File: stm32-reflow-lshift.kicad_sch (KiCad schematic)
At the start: 17 parts, among them J6 Conn_02x08_Odd_Even, Q1 2N7002, Q10 2N7002, Q11 2N7002, Q2 2N7002, Q3 2N7002, Q4 2N7002, Q5 2N7002, Q6 2N7002, Q7 2N7002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

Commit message: initial routing, added power supply source
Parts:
- J6: footprint Connector_PinSocket_2.54mm:PinSocket_2x08_P2.54mm_Vertical_SMD -> Connector_IDC:IDC-Header_2x08_P2.54mm_Vertical
- RV1: footprint Potentiometer_SMD:Potentiometer_ACP_CA6-VSMD_Vertical -> Potentiometer_SMD:Potentiometer_Bourns_3314G_Vertical
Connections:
- net DB0: now also RN2.2 (R1); no longer RN2.5 (R4)
- net DB1: now also RN2.3 (R2); no longer RN2.6 (R5)
- net DB2: now also RN2.4 (R3); no longer RN2.7 (R6)
- net DB3: now also RN2.5 (R4); no longer RN2.8 (R7)
- net DB4: now also RN2.6 (R5); no longer RN2.9 (R8)
- net DB5: now also RN2.7 (R6); no longer RN2.10 (R9)
- net DB6: now also RN2.8 (R7); no longer RN2.11 (R10)
- net DB7: now also RN2.9 (R8); no longer RN2.12 (R11)
- net E: now also RN2.12 (R11); no longer RN2.2 (R1)
- net RS: now also RN2.10 (R9); no longer RN2.4 (R3)
- net R/~{W}: now also RN2.11 (R10); no longer RN2.3 (R2)
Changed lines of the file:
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@@
     (effects (font (size 1.27 1.27)) (justify right bottom))
   )
-  (label "E" (at 38.1 110.49 270)
+  (label "DB0" (at 38.1 110.49 270)
     (effects (font (size 1.27 1.27)) (justify right bottom))
   )
@@
     (effects (font (size 1.27 1.27)) (justify left bottom))
   )
-  (label "R{slash}~{W}" (at 40.64 110.49 270)
-    (effects (font (size 1.27 1.27)) (justify right bottom))
-  )
-  (label "RS" (at 43.18 110.49 270)
-    (effects (font (size 1.27 1.27)) (justify right bottom))
-  )
-  (label "DB0" (at 45.72 110.49 270)
-    (effects (font (size 1.27 1.27)) (justify right bottom))
-  )
-  (label "DB1" (at 48.26 110.49 270)
-    (effects (font (size 1.27 1.27)) (justify right bottom))
-  )
-  (label "DB2" (at 50.8 110.49 270)
-    (effects (font (size 1.27 1.27)) (justify right bottom))
-  )
-  (label "DB3" (at 53.34 110.49 270)
-    (effects (font (size 1.27 1.27)) (justify right bottom))
-  )
-  (label "DB4" (at 55.88 110.49 270)
-    (effects (font (size 1.27 1.27)) (justify right bottom))
-  )
-  (label "DB5" (at 58.42 110.49 270)
-    (effects (font (size 1.27 1.27)) (justify right bottom))
-  )
-  (label "DB6" (at 60.96 110.49 270)
-    (effects (font (size 1.27 1.27)) (justify right bottom))
-  )
-  (label "DB7" (at 63.5 110.49 270)
+  (label "DB1" (at 40.64 110.49 270)
+    (effects (font (size 1.27 1.27)) (justify right bottom))
+  )
+  (label "DB2" (at 43.18 110.49 270)
+    (effects (font (size 1.27 1.27)) (justify right bottom))
+  )
+  (label "DB3" (at 45.72 110.49 270)
+    (effects (font (size 1.27 1.27)) (justify right bottom))
+  )
+  (label "DB4" (at 48.26 110.49 270)
+    (effects (font (size 1.27 1.27)) (justify right bottom))
+  )
+  (label "DB5" (at 50.8 110.49 270)
+    (effects (font (size 1.27 1.27)) (justify right bottom))
+  )
+  (label "DB6" (at 53.34 110.49 270)
+    (effects (font (size 1.27 1.27)) (justify right bottom))
+  )
+  (label "DB7" (at 55.88 110.49 270)
+    (effects (font (size 1.27 1.27)) (justify right bottom))
+  )
+  (label "RS" (at 58.42 110.49 270)
+    (effects (font (size 1.27 1.27)) (justify right bottom))
+  )
+  (label "R{slash}~{W}" (at 60.96 110.49 270)
+    (effects (font (size 1.27 1.27)) (justify right bottom))
+  )
+  (label "E" (at 63.5 110.49 270)
     (effects (font (size 1.27 1.27)) (justify right bottom))
   )
@@
       (effects (font (size 1.27 1.27)) (justify right))
     )
-    (property "Footprint" "Potentiometer_SMD:Potentiometer_ACP_CA6-VSMD_Vertical" (id 2) (at 31.75 55.88 0)
+    (property "Footprint" "Potentiometer_SMD:Potentiometer_Bourns_3314G_Vertical" (id 2) (at 31.75 55.88 0)
       (effects (font (size 1.27 1.27)) hide)
     )
@@
       (effects (font (size 1.27 1.27)) hide)
     )
-    (property "Footprint" "Connector_PinSocket_2.54mm:PinSocket_2x08_P2.54mm_Vertical_SMD" (id 2) (at 50.8 165.1 0)
-      (effects (font (size 1.27 1.27)) hide)
-    )
+    (property "Footprint" "Connector_IDC:IDC-Header_2x08_P2.54mm_Vertical" (id 2) (at 50.8 165.1 0)
+      (effects (font (size 1.27 1.27)) hide)
+    )

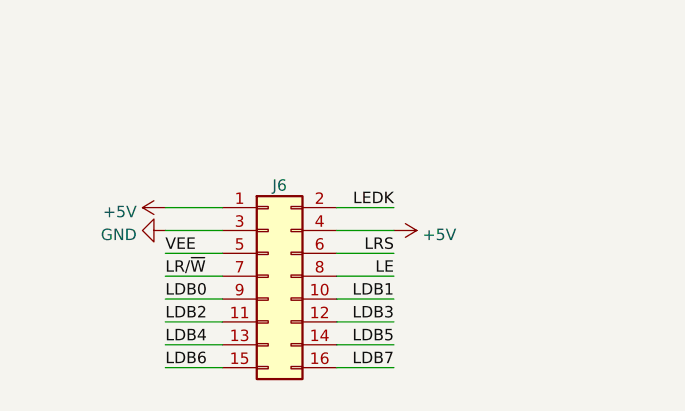
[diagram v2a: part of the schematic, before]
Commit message: fixed orientation of the LCD IDC connector
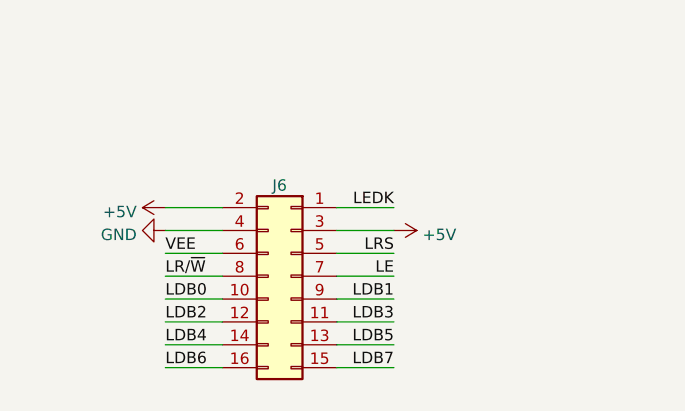
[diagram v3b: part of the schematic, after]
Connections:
- net +5V: now also J6.2 (Pin_2), J6.3 (Pin_3); no longer J6.1 (Pin_1), J6.4 (Pin_4)
- net GND: now also J6.4 (Pin_4); no longer J6.3 (Pin_3)
- net LDB0: now also J6.10 (Pin_10); no longer J6.9 (Pin_9)
- net LDB1: now also J6.9 (Pin_9); no longer J6.10 (Pin_10)
- net LDB2: now also J6.12 (Pin_12); no longer J6.11 (Pin_11)
- net LDB3: now also J6.11 (Pin_11); no longer J6.12 (Pin_12)
- net LDB4: now also J6.14 (Pin_14); no longer J6.13 (Pin_13)
- net LDB5: now also J6.13 (Pin_13); no longer J6.14 (Pin_14)
- net LDB6: now also J6.16 (Pin_16); no longer J6.15 (Pin_15)
- net LDB7: now also J6.15 (Pin_15); no longer J6.16 (Pin_16)
- net LE: now also J6.7 (Pin_7); no longer J6.8 (Pin_8)
- net LEDK: now also J6.1 (Pin_1); no longer J6.2 (Pin_2)
- net LRS: now also J6.5 (Pin_5); no longer J6.6 (Pin_6)
- net LR/~{W}: now also J6.8 (Pin_8); no longer J6.7 (Pin_7)
- net VEE: now also J6.6 (Pin_6); no longer J6.5 (Pin_5)
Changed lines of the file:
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@@
     (pin "3")
   )
-  (symbol (lib_id "Connector_Generic:Conn_02x08_Odd_Even") (at 50.8 165.1 0) (unit 1)
+  (symbol (lib_id "Connector_Generic:Conn_02x08_Odd_Even") (at 53.34 165.1 0) (mirror y) (unit 1)
     (in_bom yes) (on_board yes) (fields_autoplaced)
     (property "Reference" "J6" (id 0) (at 52.07 155.0185 0))
@@
       (effects (font (size 1.27 1.27)) hide)
     )
-    (property "Footprint" "Connector_IDC:IDC-Header_2x08_P2.54mm_Vertical" (id 2) (at 50.8 165.1 0)
+    (property "Footprint" "Connector_IDC:IDC-Header_2x08_P2.54mm_Vertical" (id 2) (at 53.34 165.1 0)
       (effects (font (size 1.27 1.27)) hide)
     )
-    (property "Datasheet" "~" (id 3) (at 50.8 165.1 0)
+    (property "Datasheet" "~" (id 3) (at 53.34 165.1 0)
       (effects (font (size 1.27 1.27)) hide)
     )

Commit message: downsized resistor network to 10
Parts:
- removed Q2: 2N7002, Package_TO_SOT_SMD:SOT-23, symbol Transistor_FET:2N7002
- removed RN1, RN2: 10k, Resistor_THT:R_Array_SIP12, symbol Device:R_Network11
- added RN1, RN2: 10k, Resistor_THT:R_Array_SIP11, symbol Device:R_Network10
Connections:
- net LR/~{W} is gone; now on net GND: J6.8 (Pin_8)
- net +5V: now also RN1.1 (common)
- net DB0: now also RN2.2 (R1)
- net DB1: now also RN2.3 (R2)
- net DB2: now also RN2.4 (R3)
- net DB3: now also RN2.5 (R4)
- net DB4: now also RN2.6 (R5)
- net DB5: now also RN2.7 (R6)
- net DB6: now also RN2.8 (R7)
- net DB7: now also RN2.9 (R8)
- net E: now also RN2.11 (R10)
- net GND: now also RN2.1 (common)
- net LDB0: now also RN1.2 (R1)
- net LDB1: now also RN1.3 (R2)
- net LDB2: now also RN1.4 (R3)
- net LDB3: now also RN1.5 (R4)
- net LDB4: now also RN1.6 (R5)
- net LDB5: now also RN1.7 (R6)
- net LDB6: now also RN1.8 (R7)
- net LDB7: now also RN1.9 (R8)
- net LE: now also RN1.11 (R10)
- net LRS: now also RN1.10 (R9)
- net RS: now also RN2.10 (R9)
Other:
- note added: "WRITE-ONLY"
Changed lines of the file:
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@@
   (junction (at 154.94 95.25) (diameter 0) (color 0 0 0 0))
   (junction (at 154.94 107.95) (diameter 0) (color 0 0 0 0))
-  (junction (at 161.29 50.6335) (diameter 0) (color 0 0 0 0))
   (junction (at 161.29 63.5) (diameter 0) (color 0 0 0 0))
   (junction (at 180.34 95.25) (diameter 0) (color 0 0 0 0))
@@
     (stroke (width 0) (type default) (color 0 0 0 0))
   )
-  (wire (pts (xy 63.5 110.49) (xy 63.5 116.84))
-    (stroke (width 0) (type default) (color 0 0 0 0))
-  )
   (wire (pts (xy 64.77 101.6) (xy 71.12 101.6))
     (stroke (width 0) (type default) (color 0 0 0 0))
@@
     (stroke (width 0) (type default) (color 0 0 0 0))
   )
-  (wire (pts (xy 101.6 45.72) (xy 161.29 45.72))
-    (stroke (width 0) (type default) (color 0 0 0 0))
-  )
-  (wire (pts (xy 104.14 40.64) (xy 104.14 43.18))
-    (stroke (width 0) (type default) (color 0 0 0 0))
-  )
-  (wire (pts (xy 104.14 43.18) (xy 186.69 43.18))
+  (wire (pts (xy 101.6 45.72) (xy 186.69 45.72))
     (stroke (width 0) (type default) (color 0 0 0 0))
   )
@@
     (stroke (width 0) (type default) (color 0 0 0 0))
   )
-  (wire (pts (xy 125.73 165.1) (xy 130.81 165.1))
-    (stroke (width 0) (type default) (color 0 0 0 0))
-  )
   (wire (pts (xy 125.73 167.64) (xy 130.81 167.64))
     (stroke (width 0) (type default) (color 0 0 0 0))
@@
     (stroke (width 0) (type default) (color 0 0 0 0))
   )
-  (wire (pts (xy 147.32 57.15) (xy 153.67 57.15))
-    (stroke (width 0) (type default) (color 0 0 0 0))
-  )
   (wire (pts (xy 154.94 86.36) (xy 154.94 95.25))
     (stroke (width 0) (type default) (color 0 0 0 0))
@@
     (stroke (width 0) (type default) (color 0 0 0 0))
   )
-  (wire (pts (xy 161.29 45.72) (xy 161.29 50.6335))
-    (stroke (width 0) (type default) (color 0 0 0 0))
-  )
-  (wire (pts (xy 161.29 50.6335) (xy 161.29 52.07))
+  (wire (pts (xy 161.29 50.6335) (xy 161.29 63.5))
     (stroke (width 0) (type default) (color 0 0 0 0))
   )
@@
     (stroke (width 0) (type default) (color 0 0 0 0))
   )
-  (wire (pts (xy 161.29 62.23) (xy 161.29 63.5))
-    (stroke (width 0) (type default) (color 0 0 0 0))
-  )
   (wire (pts (xy 161.29 63.5) (xy 186.69 63.5))
     (stroke (width 0) (type default) (color 0 0 0 0))
@@
     (stroke (width 0) (type default) (color 0 0 0 0))
   )
-  (wire (pts (xy 186.69 43.18) (xy 186.69 50.8))
+  (wire (pts (xy 186.69 45.72) (xy 186.69 50.8))
     (stroke (width 0) (type default) (color 0 0 0 0))
   )
@@
     (effects (font (size 1.27 1.27) italic) (justify left bottom))
   )
+  (text "WRITE-ONLY" (at 160.02 57.15 180)
+    (effects (font (size 1.27 1.27) italic) (justify right bottom))
+  )
   (label "LEDK" (at 25.4 21.59 270)
     (effects (font (size 1.27 1.27)) (justify right bottom))
@@
     (effects (font (size 1.27 1.27)) (justify right bottom))
   )
-  (label "R{slash}~{W}" (at 60.96 110.49 270)
-    (effects (font (size 1.27 1.27)) (justify right bottom))
-  )
-  (label "E" (at 63.5 110.49 270)
+  (label "E" (at 60.96 110.49 270)
     (effects (font (size 1.27 1.27)) (justify right bottom))
   )
@@
     (effects (font (size 1.27 1.27)) (justify right bottom))
   )
-  (label "R{slash}~{W}" (at 130.81 165.1 180)
-    (effects (font (size 1.27 1.27)) (justify right bottom))
-  )
   (label "E" (at 130.81 167.64 180)
     (effects (font (size 1.27 1.27)) (justify right bottom))
@@
   (label "LRS" (at 147.32 50.8 180)
     (effects (font (size 1.27 1.27)) (justify right bottom))
-  )
-  (label "R{slash}~{W}" (at 147.32 57.15 0)
-    (effects (font (size 1.27 1.27)) (justify left bottom))
   )
   (label "LDB3" (at 166.37 95.25 180)
@@
   )
   (hierarchical_label "RS" (shape input) (at 125.73 162.56 180)
-    (effects (font (size 1.27 1.27)) (justify right))
-  )
-  (hierarchical_label "R{slash}~{W}" (shape input) (at 125.73 165.1 180)
     (effects (font (size 1.27 1.27)) (justify right))
   )
@@
     (pin "3")
   )
-  (symbol (lib_name "2N7002_1") (lib_id "Transistor_FET:2N7002") (at 158.75 57.15 0) (unit 1)
-    (in_bom yes) (on_board yes) (fields_autoplaced)
-    (property "Reference" "Q2" (id 0) (at 163.9824 56.2415 0)
-      (effects (font (size 1.27 1.27)) (justify left))
-    )
-    (property "Value" "2N7002" (id 1) (at 163.9824 59.0166 0)
-      (effects (font (size 1.27 1.27)) (justify left))
-    )
-    (property "Footprint" "Package_TO_SOT_SMD:SOT-23" (id 2) (at 163.83 59.055 0)
-      (effects (font (size 1.27 1.27) italic) (justify left) hide)
-    )
-    (property "Datasheet" "https://www.fairchildsemi.com/datasheets/2N/2N7002.pdf" (id 3) (at 158.75 57.15 0)
-      (effects (font (size 1.27 1.27)) (justify left) hide)
-    )
-    (pin "1")
-    (pin "2")
-    (pin "3")
-  )
   (symbol (lib_id "Transistor_FET:2N7002") (at 177.8 101.6 0) (unit 1)
     (in_bom yes) (on_board yes) (fields_autoplaced)
@@
     (pin "2")
     (pin "3")
+  )
+  (symbol (lib_id "Device:R_Network10") (at 50.8 121.92 0) (mirror x) (unit 1)
+    (in_bom yes) (on_board yes) (fields_autoplaced)
+    (property "Reference" "RN2" (id 0) (at 36.068 121.0115 0)
+      (effects (font (size 1.27 1.27)) (justify right))
+    )
+    (property "Value" "10k" (id 1) (at 36.068 123.7866 0)
+      (effects (font (size 1.27 1.27)) (justify right))
+    )
+    (property "Footprint" "Resistor_THT:R_Array_SIP11" (id 2) (at 65.405 121.92 90)
+      (effects (font (size 1.27 1.27)) hide)
+    )
+    (property "Datasheet" "http://www.vishay.com/docs/31509/csc.pdf" (id 3) (at 50.8 121.92 0)
+      (effects (font (size 1.27 1.27)) hide)
+    )
+    (pin "1")
+    (pin "10")
+    (pin "11")
+    (pin "2")
+    (pin "3")
+    (pin "4")
+    (pin "5")
+    (pin "6")
+    (pin "7")
+    (pin "8")
+    (pin "9")
+  )
+  (symbol (lib_id "Device:R_Network10") (at 91.44 35.56 0) (unit 1)
+    (in_bom yes) (on_board yes) (fields_autoplaced)
+    (property "Reference" "RN1" (id 0) (at 103.632 34.6515 0)
+      (effects (font (size 1.27 1.27)) (justify left))
+    )
+    (property "Value" "10k" (id 1) (at 103.632 37.4266 0)
+      (effects (font (size 1.27 1.27)) (justify left))
+    )
+    (property "Footprint" "Resistor_THT:R_Array_SIP11" (id 2) (at 106.045 35.56 90)
+      (effects (font (size 1.27 1.27)) hide)
+    )
+    (property "Datasheet" "http://www.vishay.com/docs/31509/csc.pdf" (id 3) (at 91.44 35.56 0)
+      (effects (font (size 1.27 1.27)) hide)
+    )
+    (pin "1")
+    (pin "10")
+    (pin "11")
+    (pin "2")
+    (pin "3")
+    (pin "4")
+    (pin "5")
+    (pin "6")
+    (pin "7")
+    (pin "8")
+    (pin "9")
   )
   (symbol (lib_id "Connector_Generic:Conn_02x08_Odd_Even") (at 53.34 165.1 0) (mirror y) (unit 1)
@@
     (pin "2")
     (pin "3")
-    (pin "4")
-    (pin "5")
-    (pin "6")
-    (pin "7")
-    (pin "8")
-    (pin "9")
-  )
-  (symbol (lib_id "Device:R_Network11") (at 50.8 121.92 0) (mirror x) (unit 1)
-    (in_bom yes) (on_board yes) (fields_autoplaced)
-    (property "Reference" "RN2" (id 0) (at 36.068 121.0115 0)
-      (effects (font (size 1.27 1.27)) (justify right))
-    )
-    (property "Value" "10k" (id 1) (at 36.068 123.7866 0)
-      (effects (font (size 1.27 1.27)) (justify right))
-    )
-    (property "Footprint" "Resistor_THT:R_Array_SIP12" (id 2) (at 67.945 121.92 90)
-      (effects (font (size 1.27 1.27)) hide)
-    )
-    (property "Datasheet" "http://www.vishay.com/docs/31509/csc.pdf" (id 3) (at 50.8 121.92 0)
-      (effects (font (size 1.27 1.27)) hide)
-    )
-    (pin "1")
-    (pin "10")
-    (pin "11")
-    (pin "12")
-    (pin "2")
-    (pin "3")
-    (pin "4")
-    (pin "5")
-    (pin "6")
-    (pin "7")
-    (pin "8")
-    (pin "9")
-  )
-  (symbol (lib_id "Device:R_Network11") (at 91.44 35.56 0) (unit 1)
-    (in_bom yes) (on_board yes) (fields_autoplaced)
-    (property "Reference" "RN1" (id 0) (at 106.172 34.6515 0)
-      (effects (font (size 1.27 1.27)) (justify left))
-    )
-    (property "Value" "10k" (id 1) (at 106.172 37.4266 0)
-      (effects (font (size 1.27 1.27)) (justify left))
-    )
-    (property "Footprint" "Resistor_THT:R_Array_SIP12" (id 2) (at 108.585 35.56 90)
-      (effects (font (size 1.27 1.27)) hide)
-    )
-    (property "Datasheet" "http://www.vishay.com/docs/31509/csc.pdf" (id 3) (at 91.44 35.56 0)
-      (effects (font (size 1.27 1.27)) hide)
-    )
-    (pin "1")
-    (pin "10")
-    (pin "11")
-    (pin "12")
-    (pin "2")
-    (pin "3")
